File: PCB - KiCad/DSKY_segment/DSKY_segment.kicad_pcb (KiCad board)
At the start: 2 copper layers, 62.4 x 105.7 mm, 3 parts, among them J1 Conn_15X4, J2 Conn_15X4, J3 Conn_15X4

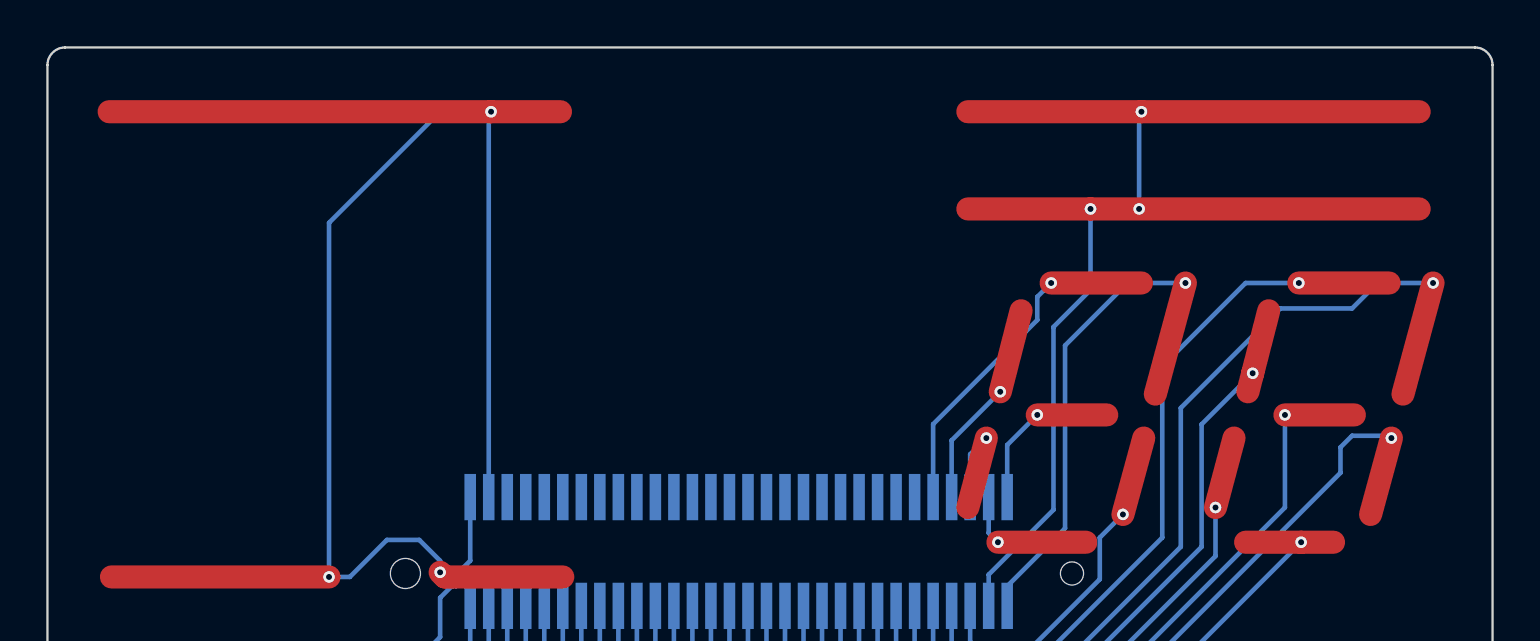
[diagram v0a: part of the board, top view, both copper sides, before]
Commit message: Modified layout to support common electrode
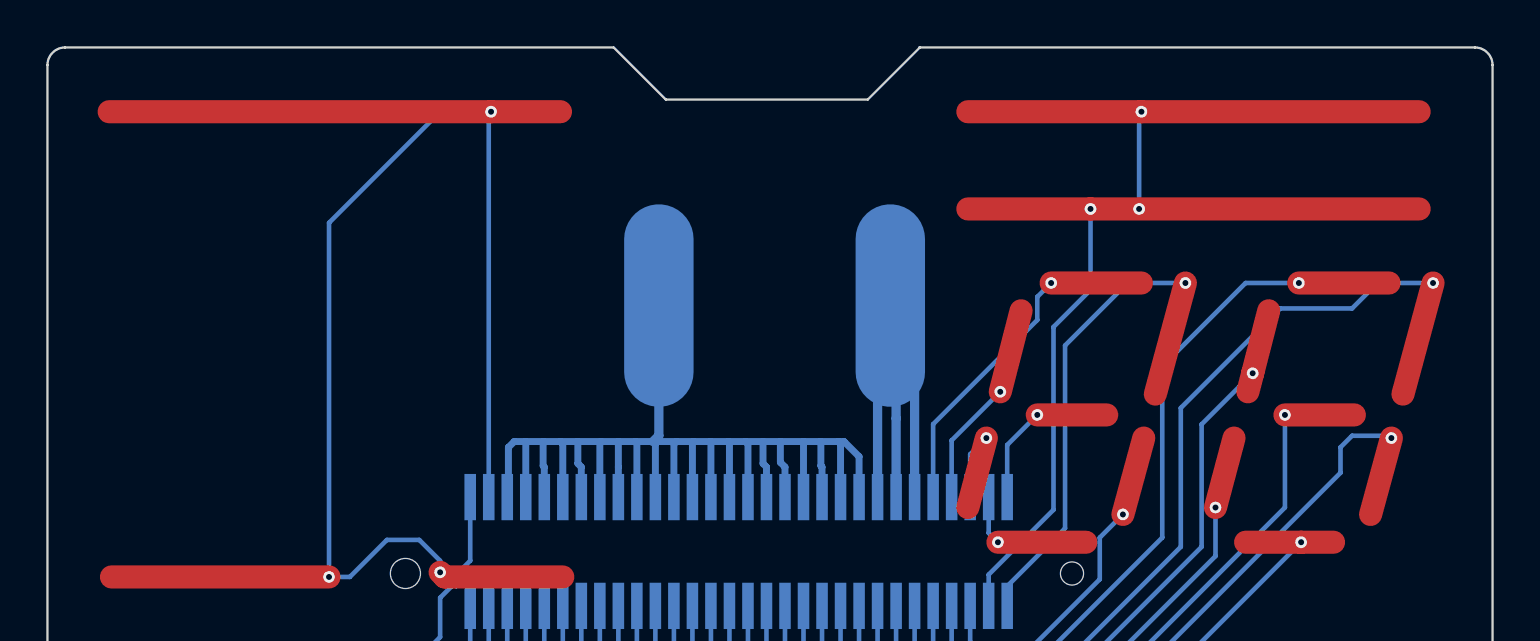
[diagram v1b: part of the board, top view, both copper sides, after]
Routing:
- net (no net): track 3507.0 -> 3602.4 mm
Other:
- outline, holes or cut-outs redrawn
- board text added: "COMMON"
- board text added: "GND"
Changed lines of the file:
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@@
-(kicad_pcb (version 20171130) (host pcbnew "(5.1.0)-1")
+(kicad_pcb (version 20171130) (host pcbnew "(5.0.0)")
   (general
     (thickness 1.6)
-    (drawings 680)
-    (tracks 1131)
+    (drawings 688)
+    (tracks 1206)
     (zones 0)
     (modules 3)
@@
   )
   (setup
-    (last_trace_width 0.2)
+    (last_trace_width 3)
+    (user_trace_width 0.3)
+    (user_trace_width 0.4)
     (user_trace_width 0.75)
     (user_trace_width 1)
+    (user_trace_width 3)
     (trace_clearance 0.2)
     (zone_clearance 0.508)
     (zone_45_only no)
     (trace_min 0.2)
+    (segment_width 3.2)
+    (edge_width 0.1)
     (via_size 0.508)
     (via_drill 0.254)
@@
     (uvia_min_size 0.2)
     (uvia_min_drill 0.1)
-    (edge_width 0.15)
-    (segment_width 0.2)
     (pcb_text_width 0.3)
     (pcb_text_size 1.5 1.5)
@@
     (pad "" np_thru_hole circle (at -14.4 0.95) (size 1.3 1.3) (drill 1.3) (layers *.Cu *.Mask))
   )
-  (gr_text FX6-60P (at 157.2 43.7) (layer B.SilkS)
+  (gr_text COMMON (at 150.25 38 90) (layer B.SilkS)
+    (effects (font (size 1.5 1.5) (thickness 0.2)) (justify mirror))
+  )
+  (gr_line (start 157.25 41.25) (end 157.25 35.5) (layer B.Mask) (width 3.2))
+  (gr_line (start 147.25 41.25) (end 147.25 35.5) (layer B.Mask) (width 3.2))
+  (gr_line (start 156.275 29.475) (end 158.525 27.225) (layer Edge.Cuts) (width 0.1))
+  (gr_line (start 147.55 29.475) (end 156.275 29.475) (layer Edge.Cuts) (width 0.1))
+  (gr_line (start 145.3 27.225) (end 147.55 29.475) (layer Edge.Cuts) (width 0.1))
+  (gr_line (start 158.495958 27.223) (end 182.508 27.223) (layer Edge.Cuts) (width 0.1))
+  (gr_text GND (at 160.5 38.25 90) (layer B.SilkS)
+    (effects (font (size 1.5 1.5) (thickness 0.2)) (justify mirror))
+  )
+  (gr_text FX6-60P (at 141.475 54.05) (layer B.SilkS)
     (effects (font (size 1 1) (thickness 0.15)) (justify mirror))
   )
@@
   (gr_line (start 120.834 132.204) (end 120.834 27.985) (layer Edge.Cuts) (width 0.1))
   (gr_line (start 183.27 27.985) (end 183.27 132.204) (layer Edge.Cuts) (width 0.1))
-  (gr_line (start 121.596 27.223) (end 182.508 27.223) (layer Edge.Cuts) (width 0.1))
+  (gr_line (start 121.596 27.223) (end 145.288921 27.223) (layer Edge.Cuts) (width 0.1))
   (gr_arc (start 182.508 27.985) (end 183.27 27.985) (angle -90) (layer Edge.Cuts) (width 0.1))
   (gr_arc (start 121.596 132.204) (end 120.834 132.204) (angle -90) (layer Edge.Cuts) (width 0.1))
@@
   (segment (start 167.2 87.9) (end 167.2 86.9) (width 0.2) (layer B.Cu) (net 0))
   (segment (start 164.6 90.5) (end 167.2 87.9) (width 0.2) (layer B.Cu) (net 0))
+  (segment (start 157.5 46.65) (end 157.5 43.25) (width 0.4) (layer B.Cu) (net 0))
+  (segment (start 156.7 46.65) (end 156.7 41.8) (width 0.4) (layer B.Cu) (net 0))
+  (segment (start 157.5 43.25) (end 157.5 41) (width 0.4) (layer B.Cu) (net 0))
+  (segment (start 158.3 41.8) (end 157.5 41) (width 0.4) (layer B.Cu) (net 0))
+  (segment (start 158.3 46.65) (end 158.3 41.8) (width 0.4) (layer B.Cu) (net 0))
+  (segment (start 140.7 45.9) (end 140.75 45.85) (width 0.3) (layer B.Cu) (net 0))
+  (segment (start 140.7 46.65) (end 140.7 45.9) (width 0.3) (layer B.Cu) (net 0))
+  (segment (start 140.75 45.85) (end 140.75 44.5) (width 0.3) (layer B.Cu) (net 0))
+  (segment (start 140.75 44.5) (end 141 44.25) (width 0.3) (layer B.Cu) (net 0))
+  (segment (start 155.9 44.9) (end 155.9 46.65) (width 0.3) (layer B.Cu) (net 0))
+  (segment (start 155.25 44.25) (end 155.9 44.9) (width 0.3) (layer B.Cu) (net 0))
+  (segment (start 141.5 46.65) (end 141.5 44.25) (width 0.3) (layer B.Cu) (net 0))
+  (segment (start 141 44.25) (end 141.5 44.25) (width 0.3) (layer B.Cu) (net 0))
+  (segment (start 142.25 45.3) (end 142.25 44.25) (width 0.3) (layer B.Cu) (net 0))
+  (segment (start 142.3 45.35) (end 142.25 45.3) (width 0.3) (layer B.Cu) (net 0))
+  (segment (start 142.3 46.65) (end 142.3 45.35) (width 0.3) (layer B.Cu) (net 0))
+  (segment (start 141.5 44.25) (end 142.25 44.25) (width 0.3) (layer B.Cu) (net 0))
+  (segment (start 143.1 44.35) (end 143 44.25) (width 0.3) (layer B.Cu) (net 0))
+  (segment (start 143.1 46.65) (end 143.1 44.35) (width 0.3) (layer B.Cu) (net 0))
+  (segment (start 142.25 44.25) (end 143 44.25) (width 0.3) (layer B.Cu) (net 0))
+  (segment (start 143.75 45.2) (end 143.75 44.25) (width 0.3) (layer B.Cu) (net 0))
+  (segment (start 143.9 45.35) (end 143.75 45.2) (width 0.3) (layer B.Cu) (net 0))
+  (segment (start 143.9 46.65) (end 143.9 45.35) (width 0.3) (layer B.Cu) (net 0))
+  (segment (start 143 44.25) (end 143.75 44.25) (width 0.3) (layer B.Cu) (net 0))
+  (segment (start 144.7 44.3) (end 144.75 44.25) (width 0.3) (layer B.Cu) (net 0))
+  (segment (start 144.7 46.65) (end 144.7 44.3) (width 0.3) (layer B.Cu) (net 0))
+  (segment (start 143.75 44.25) (end 144.75 44.25) (width 0.3) (layer B.Cu) (net 0))
+  (segment (start 145.5 45.35) (end 145.5 44.25) (width 0.3) (layer B.Cu) (net 0))
+  (segment (start 145.5 46.65) (end 145.5 45.35) (width 0.3) (layer B.Cu) (net 0))
+  (segment (start 144.75 44.25) (end 145.5 44.25) (width 0.3) (layer B.Cu) (net 0))
+  (segment (start 146.3 44.3) (end 146.25 44.25) (width 0.3) (layer B.Cu) (net 0))
+  (segment (start 146.3 46.65) (end 146.3 44.3) (width 0.3) (layer B.Cu) (net 0))
+  (segment (start 145.5 44.25) (end 146.25 44.25) (width 0.3) (layer B.Cu) (net 0))
+  (segment (start 147.1 44.35) (end 147 44.25) (width 0.3) (layer B.Cu) (net 0))
+  (segment (start 147.1 46.65) (end 147.1 44.35) (width 0.3) (layer B.Cu) (net 0))
+  (segment (start 146.25 44.25) (end 147 44.25) (width 0.3) (layer B.Cu) (net 0))
+  (segment (start 147.9 44.35) (end 148 44.25) (width 0.3) (layer B.Cu) (net 0))
+  (segment (start 147.9 46.65) (end 147.9 44.35) (width 0.3) (layer B.Cu) (net 0))
+  (segment (start 147 44.25) (end 148 44.25) (width 0.3) (layer B.Cu) (net 0))
+  (segment (start 148.7 44.3) (end 148.75 44.25) (width 0.3) (layer B.Cu) (net 0))
+  (segment (start 148.7 46.65) (end 148.7 44.3) (width 0.3) (layer B.Cu) (net 0))
+  (segment (start 148 44.25) (end 148.75 44.25) (width 0.3) (layer B.Cu) (net 0))
+  (segment (start 149.5 46.65) (end 149.5 44.25) (width 0.3) (layer B.Cu) (net 0))
+  (segment (start 148.75 44.25) (end 149.5 44.25) (width 0.3) (layer B.Cu) (net 0))
+  (segment (start 150.3 44.3) (end 150.25 44.25) (width 0.3) (layer B.Cu) (net 0))
+  (segment (start 150.3 46.65) (end 150.3 44.3) (width 0.3) (layer B.Cu) (net 0))
+  (segment (start 149.5 44.25) (end 150.25 44.25) (width 0.3) (layer B.Cu) (net 0))
+  (segment (start 151.1 44.35) (end 151 44.25) (width 0.3) (layer B.Cu) (net 0))
+  (segment (start 151.1 46.65) (end 151.1 44.35) (width 0.3) (layer B.Cu) (net 0))
+  (segment (start 150.25 44.25) (end 151 44.25) (width 0.3) (layer B.Cu) (net 0))
+  (segment (start 151.75 45.2) (end 151.75 44.25) (width 0.3) (layer B.Cu) (net 0))
+  (segment (start 151.9 45.35) (end 151.75 45.2) (width 0.3) (layer B.Cu) (net 0))
+  (segment (start 151.9 46.65) (end 151.9 45.35) (width 0.3) (layer B.Cu) (net 0))
+  (segment (start 151 44.25) (end 151.75 44.25) (width 0.3) (layer B.Cu) (net 0))
+  (segment (start 152.5 45.15) (end 152.5 44.25) (width 0.3) (layer B.Cu) (net 0))
+  (segment (start 152.7 45.35) (end 152.5 45.15) (width 0.3) (layer B.Cu) (net 0))
+  (segment (start 152.7 46.65) (end 152.7 45.35) (width 0.3) (layer B.Cu) (net 0))
+  (segment (start 151.75 44.25) (end 152.5 44.25) (width 0.3) (layer B.Cu) (net 0))
+  (segment (start 153.5 45.9) (end 153.5 44.25) (width 0.3) (layer B.Cu) (net 0))
+  (segment (start 153.5 46.65) (end 153.5 45.9) (width 0.3) (layer B.Cu) (net 0))
+  (segment (start 152.5 44.25) (end 153.5 44.25) (width 0.3) (layer B.Cu) (net 0))
+  (segment (start 154.25 45.3) (end 154.25 44.25) (width 0.3) (layer B.Cu) (net 0))
+  (segment (start 154.3 45.35) (end 154.25 45.3) (width 0.3) (layer B.Cu) (net 0))
+  (segment (start 154.3 46.65) (end 154.3 45.35) (width 0.3) (layer B.Cu) (net 0))
+  (segment (start 153.5 44.25) (end 154.25 44.25) (width 0.3) (layer B.Cu) (net 0))
+  (segment (start 155.1 44.35) (end 155 44.25) (width 0.3) (layer B.Cu) (net 0))
+  (segment (start 155.1 46.65) (end 155.1 44.35) (width 0.3) (layer B.Cu) (net 0))
+  (segment (start 154.25 44.25) (end 155 44.25) (width 0.3) (layer B.Cu) (net 0))
+  (segment (start 155 44.25) (end 155.25 44.25) (width 0.3) (layer B.Cu) (net 0))
+  (segment (start 147.25 35.5) (end 147.25 41.25) (width 3) (layer B.Cu) (net 0))
+  (segment (start 147.25 44) (end 147 44.25) (width 0.4) (layer B.Cu) (net 0))
+  (segment (start 147.25 41.25) (end 147.25 44) (width 0.4) (layer B.Cu) (net 0))
+  (segment (start 157.25 35.5) (end 157.25 41.25) (width 3) (layer B.Cu) (net 0))
+  (segment (start 156.7 41.8) (end 157.25 41.25) (width 0.4) (layer B.Cu) (net 0))
+  (segment (start 157.25 41.25) (end 157.5 41) (width 0.4) (layer B.Cu) (net 0))
 )

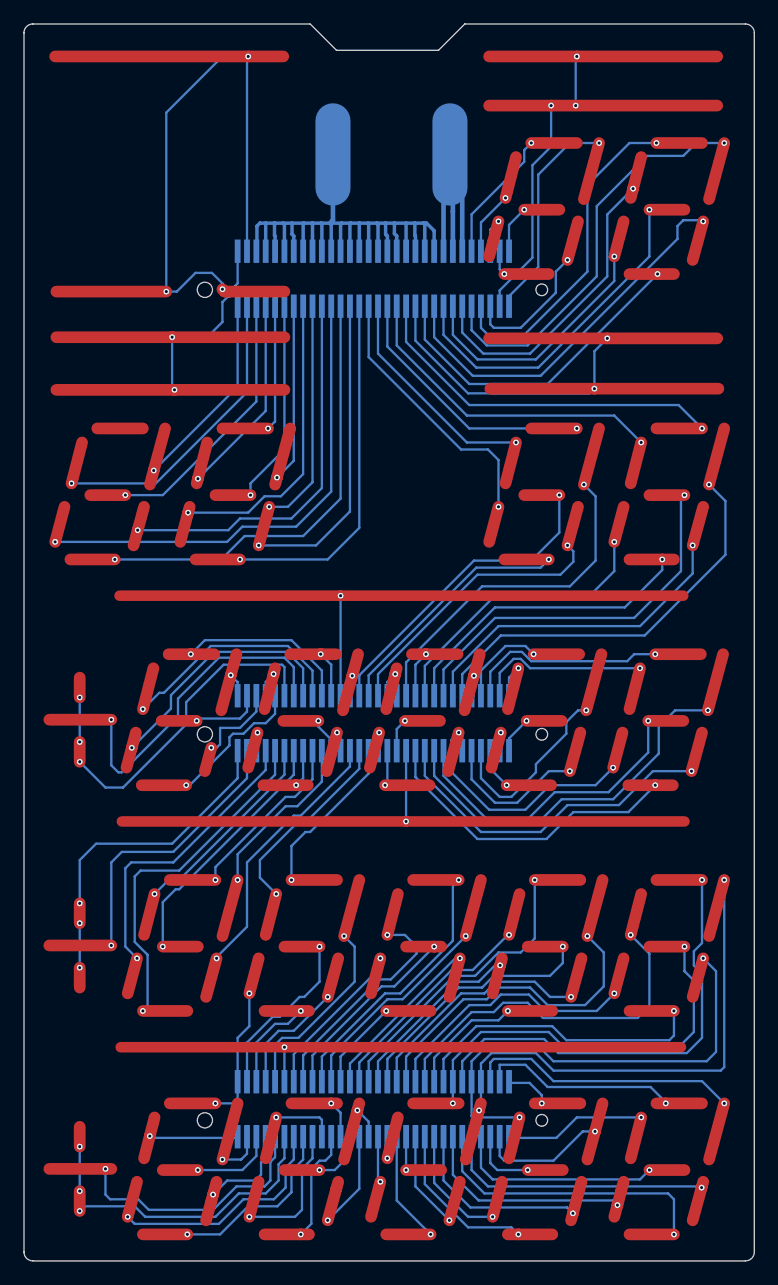
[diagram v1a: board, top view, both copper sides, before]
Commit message: V3 of PCB hardware
3.3 to 5V level shifter added
Added decoupling caps to 5V rail and HV rail
Added cap to RESET line
Fixed locating holes in FX6 footprint
Fixed unintentional trace overlap
Eliminated the "GND" feature, and re-assigned all lines to be the common electrode
Fixed a routing error on the segment PCB, and re-assigned one common electrode line to be a segment line.
The above changes mean that the common electrode mask in firmware *must* be updated.
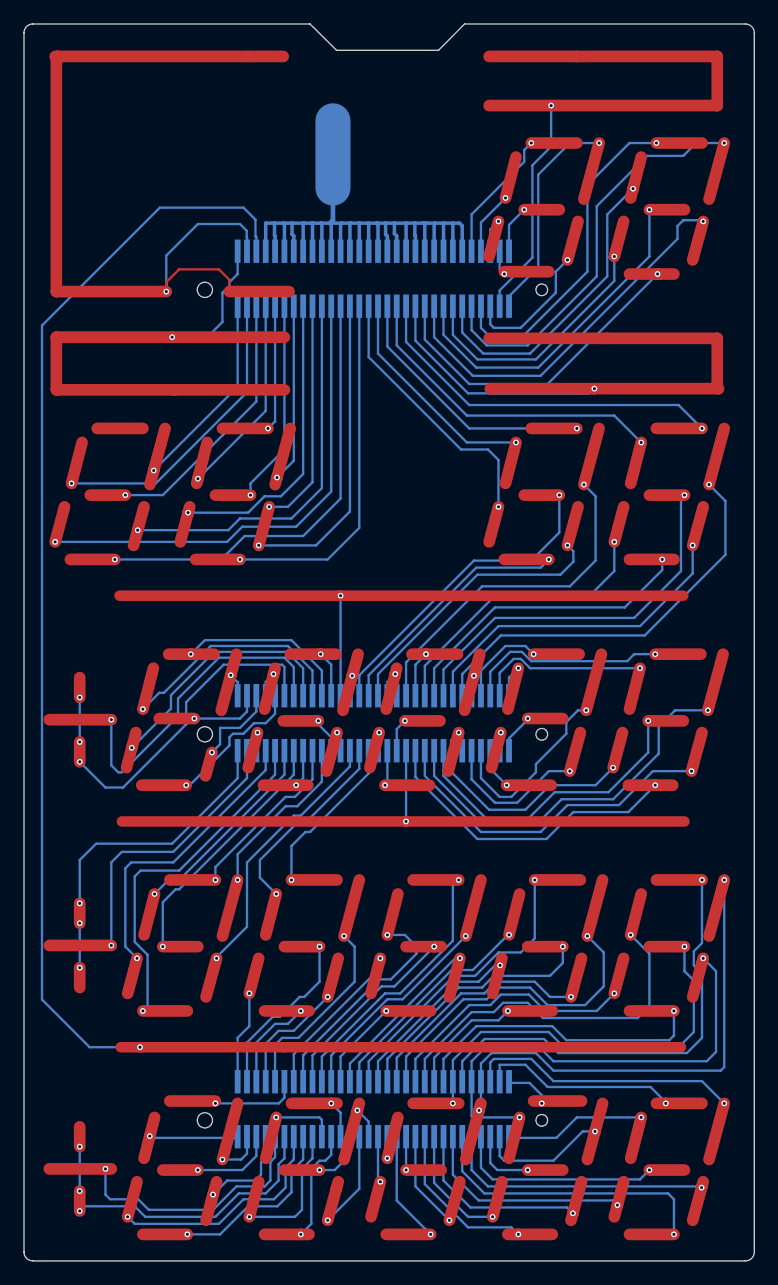
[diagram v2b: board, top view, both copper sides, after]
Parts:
- added LOGO1: Logo_Open_Hardware_Large, Symbol:OSHW-Logo2_7.3x6mm_SilkScreen, B.Cu at (125.3, 31.4)
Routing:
- net (no net): track 3602.4 -> 3673.8 mm, vias 172 -> 166
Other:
- board text added: "042119"
- board text added: "DSKY_V3_SEG"
- board text removed: "04012019"
- board text removed: "DSKY_V2_SEG"
- board text removed: "GND"

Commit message: V4 of segment PCB
Routing fixes.  Added protection diode for common electrode
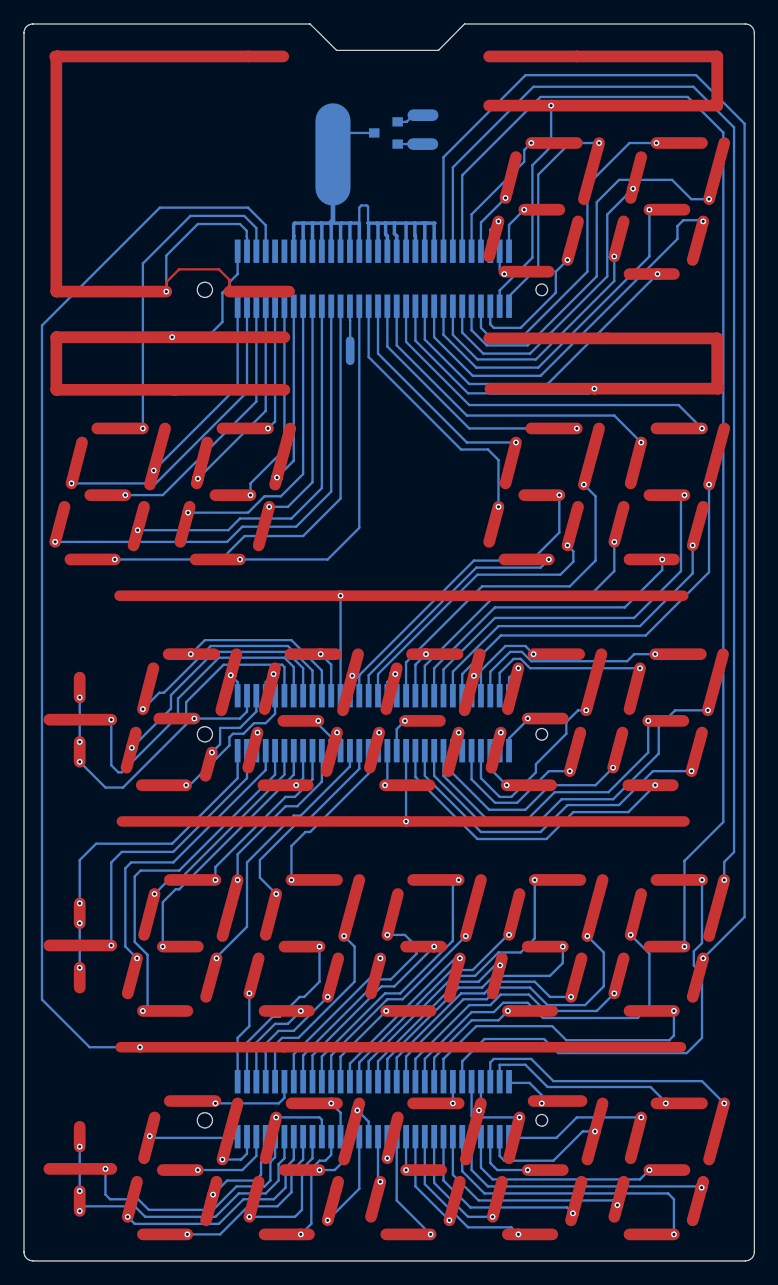
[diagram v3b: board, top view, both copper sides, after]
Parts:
- added D1: MMBD5004S, Package_TO_SOT_SMD:SOT-23, B.Cu at (151.8, 36.5)
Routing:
- net (no net): track 3673.8 -> 3871.3 mm
- net Net-(D1-Pad3): track 0.00 -> 3.96 mm
- net Net-(D1-Pad1): track 0.00 -> 3.23 mm
- net Net-(D1-Pad2): track 0.00 -> 2.97 mm
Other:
- board text added: "050519"
- board text added: "DSKY_V4_SEG"
- board text added: "GND"
- board text added: "HV +"
- board text removed: "042119"
- board text removed: "DSKY_V3_SEG"
